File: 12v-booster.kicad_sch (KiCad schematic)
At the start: 21 parts, among them J409 12V_OUT, U201 XCL220, U405 TPS55340-Q1

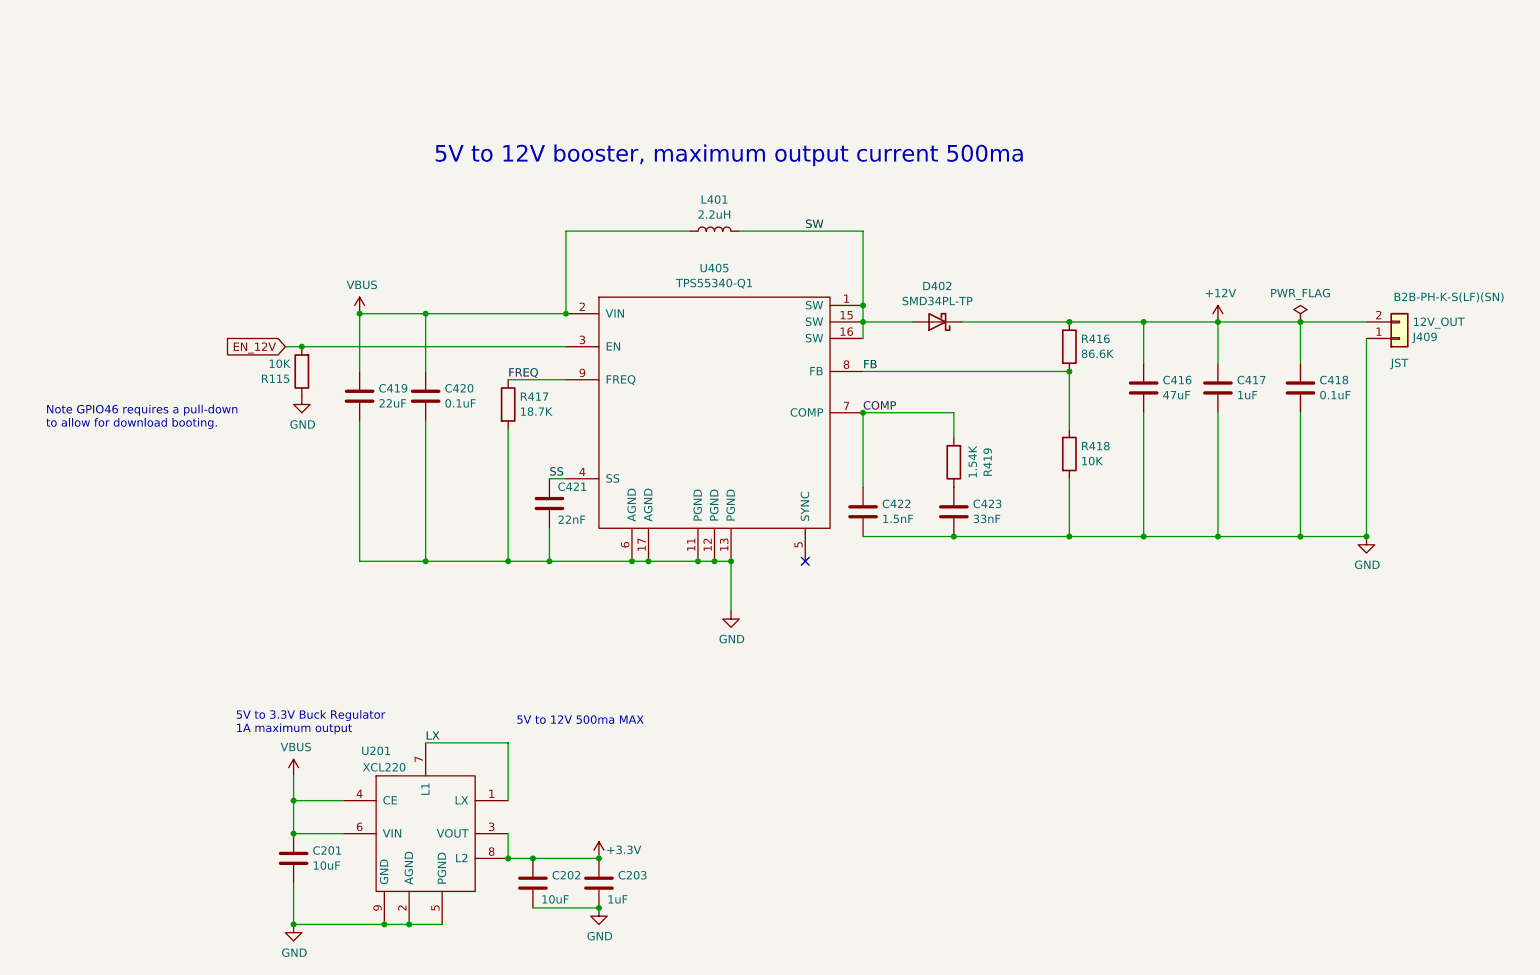
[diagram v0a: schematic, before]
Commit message: More updates
- Changed obsolete unidirectional level shifter to open-collector level shifter
- Replaced BSS138 level shifters with dedicated level shifter
- Changed all 5V I/O pins to have 33 ohm resistor in series
- Changed a few capacitors
- Cleanup tracks, vias, silkscreen, etc.

Signed-off-by: Aaron Williams <aaron.w2@gmail.com>
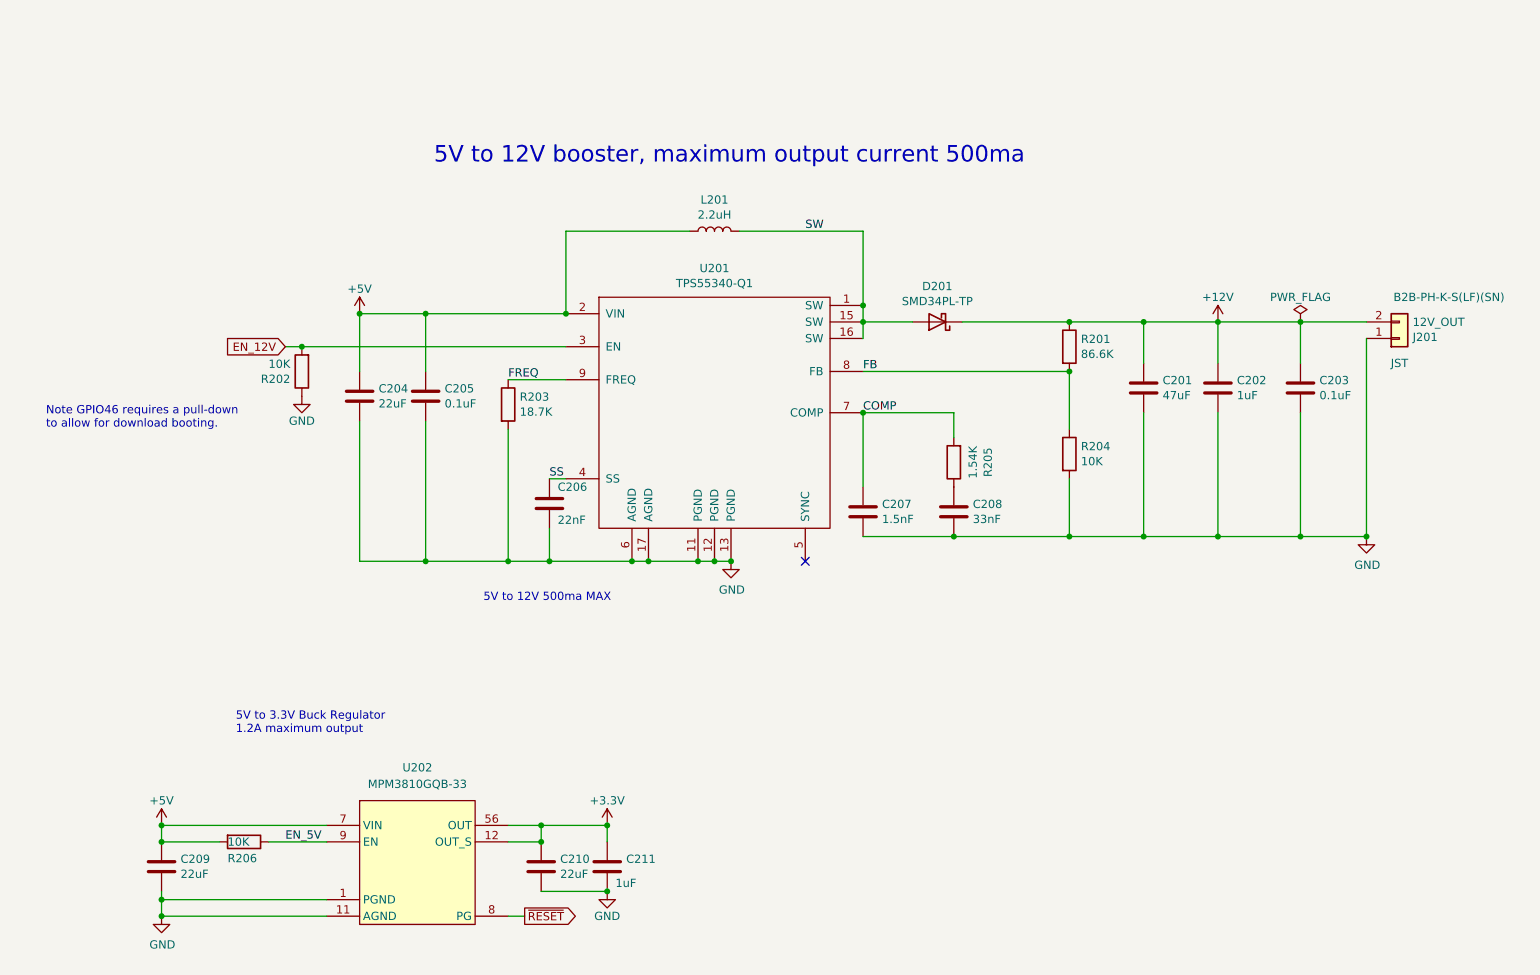
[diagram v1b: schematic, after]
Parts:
- removed C201, C202: 10uF, Capacitor_SMD:C_0603_1608Metric, symbol Device:C
- removed U201: XCL220, Torex_Semi:CL-2025-02, symbol led-controller-wrover32-rescue:XCL21X-Torex_Semiconductor
- added C209, C210: 22uF, Capacitor_SMD:C_0603_1608Metric, symbol Device:C
- added R206: 10K, Resistor_SMD:R_0402_1005Metric, symbol Device:R
- added U202: MPM3810GQB-33, Package_DFN_QFN:Monolithic_QFN-12-2.5x3.0mm_P0.4mm, symbol Power_Management:MPM3810GQB-33
- renumbered C416 to C201, C417 to C202, C418 to C203, C419 to C204, C420 to C205, C421 to C206, C422 to C207, C423 to C208, C203 to C211, D402 to D201, J409 to J201, L401 to L201, R416 to R201, R115 to R202, R417 to R203, R418 to R204, R419 to R205, U405 to U201
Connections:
- net +3V3: now also C210.1, U202.12 (OUT_S), U202.56 (OUT)
- net GND: now also C209.2, C210.2, U202.1 (PGND), U202.11 (AGND), U202.2 (PGND)
- net VBUS renamed +5V
- net +5V: now also C209.1, R206.2, U202.7 (VIN)
- new net EN_5V: R206.1, U202.9 (EN)
- new net ~{RESET}: U202.8 (PG)
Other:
- note added: "5V to 3.3V Buck Regulator 1.2A maximum output"
- note removed: "5V to 3.3V Buck Regulator 1A maximum output"
- moved on the sheet: C211

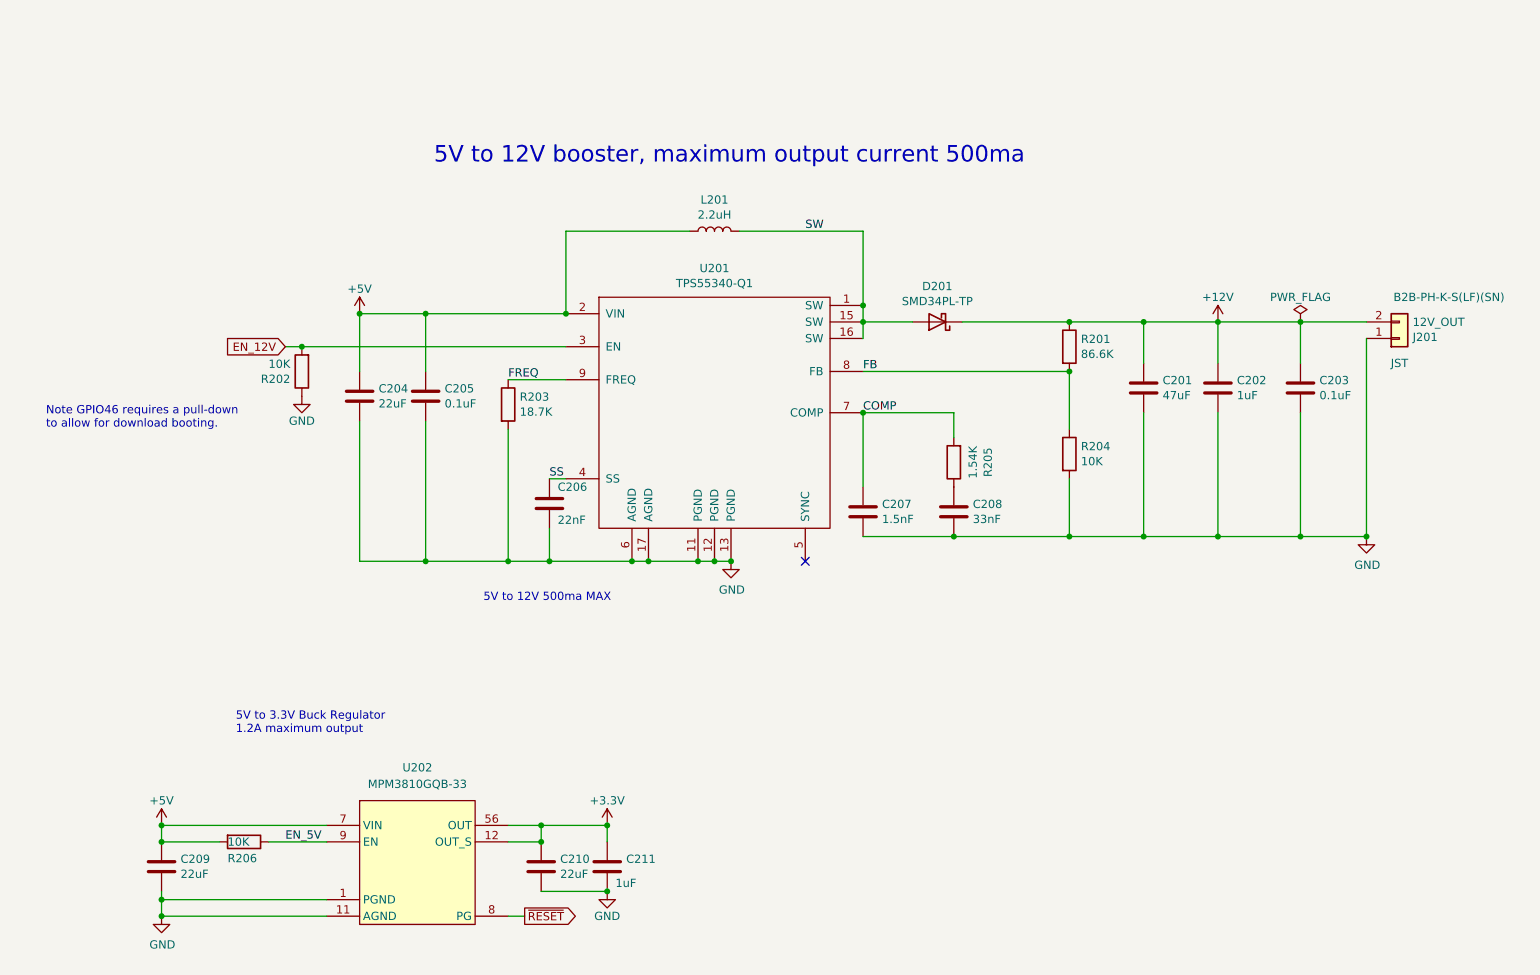
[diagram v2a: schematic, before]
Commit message: Switched to a different 12V booster chip and increased 12V from 500ma to 1A.
Also:
- Switched most 10uF capacitors to 0402 footprints.
- Other cleanup

Signed-off-by: Aaron Williams <aaron.w2@gmail.com>
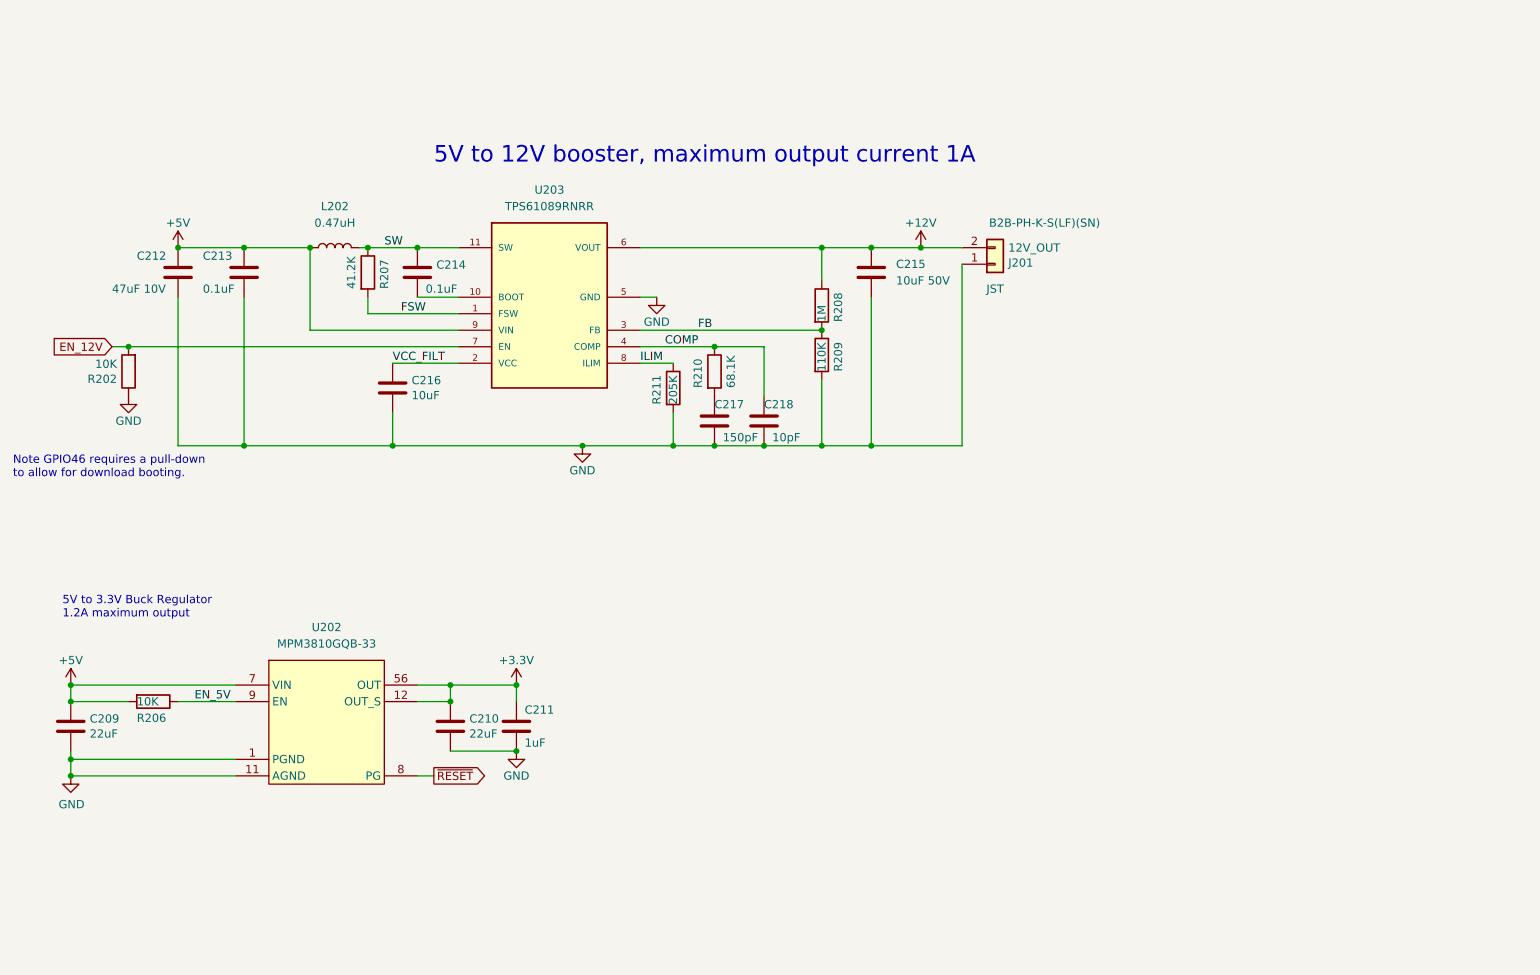
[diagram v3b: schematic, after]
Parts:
- removed C201: 47uF, Capacitor_SMD:C_1210_3225Metric, symbol Device:C
- removed C202: 1uF, Capacitor_SMD:C_0402_1005Metric, symbol Device:C
- removed C203, C205: 0.1uF, Capacitor_SMD:C_0402_1005Metric, symbol Device:C
- removed C204: 22uF, Capacitor_SMD:C_0603_1608Metric, symbol Device:C
- removed C206: 22nF, Capacitor_SMD:C_0402_1005Metric, symbol Device:C
- removed C207: 1.5nF, Capacitor_SMD:C_0402_1005Metric, symbol Device:C
- removed C208: 33nF, Capacitor_SMD:C_0402_1005Metric, symbol Device:C
- removed D201: SMD34PL-TP, Diode_SMD:D_SOD-123F, symbol Device:D_Schottky
- removed L201: 2.2uH, Inductor_SMD:L_1210_3225Metric, symbol Device:L
- removed R201: 86.6K, Resistor_SMD:R_0402_1005Metric, symbol Device:R
- removed R203: 18.7K, Resistor_SMD:R_0402_1005Metric, symbol Device:R
- removed R204: 10K, Resistor_SMD:R_0402_1005Metric, symbol Device:R
- removed R205: 1.54K, Resistor_SMD:R_0402_1005Metric, symbol Device:R
- removed U201: TPS55340-Q1, Aaron:QFN-16-1EP_3x3mm_P0.5mm_EP2.7x2.7mm_ThermalVias, symbol led-controller-wrover32-rescue:TPS55340-Q1-texas-12v-booster-rescue
- added C212: 47uF 10V, Capacitor_SMD:C_0805_2012Metric, symbol Device:C
- added C213, C214: 0.1uF, Capacitor_SMD:C_0402_1005Metric, symbol Device:C
- added C215: 10uF 50V, Capacitor_SMD:C_0805_2012Metric, symbol Device:C
- added C216: 10uF, Capacitor_SMD:C_0402_1005Metric, symbol Device:C
- added C217: 150pF, Capacitor_SMD:C_0402_1005Metric, symbol Device:C
- added C218: 10pF, Capacitor_SMD:C_0402_1005Metric, symbol Device:C
- added L202: 0.47uH, Inductor_SMD:L_Bourns_SRP3212, symbol Device:L
- added R207: 41.2K, Resistor_SMD:R_0402_1005Metric, symbol Device:R
- added R208: 1M, Resistor_SMD:R_0402_1005Metric, symbol Device:R
- added R209: 110K, Resistor_SMD:R_0402_1005Metric, symbol Device:R
- added R210: 68.1K, Resistor_SMD:R_0402_1005Metric, symbol Device:R
- added R211: 205K, Resistor_SMD:R_0402_1005Metric, symbol Device:R
- added U203: TPS61089RNRR, Package_DFN_QFN:Texas_S_VQFN-11_2.0x2.5mm_P0.5mm_Thermal, symbol Aaron:TPS61089RNRR
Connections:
- net +12V: now also C215.1, R208.1, U203.6 (VOUT)
- net +5V: now also C212.1, C213.1, L202.1, U203.9 (VIN)
- net COMP: now also C218.1, R210.1, U203.4 (COMP)
- net EN_12V: now also U203.7 (EN)
- net FB: now also R208.2, R209.1, U203.3 (FB)
- net GND: now also C212.2, C213.2, C215.2, C216.2, C217.2, C218.2, R209.2, R211.2, U203.5 (GND)
- net SW: now also C214.1, L202.2, R207.1, U203.11 (SW)
- new net: C217.1, R210.2
- new net: C214.2, U203.10 (BOOT)
- new net FSW: R207.2, U203.1 (FSW)
- new net ILIM: R211.1, U203.8 (ILIM)
- new net VCC_FILT: C216.1, U203.2 (VCC)
- no-connect marks 1 -> 0
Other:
- note added: "5V to 12V booster, maximum output current 1A"
- note removed: "5V to 12V 500ma MAX"
- note removed: "5V to 12V booster, maximum output current 500ma"
- moved on the sheet: C209, C210, C211, J201, R202, R206, U202

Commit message: Latest 4.0 settings for pcbway
Signed-off-by: Aaron Williams <aaron.w2@gmail.com>
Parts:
- removed R202: 10K, Resistor_SMD:R_0402_1005Metric, symbol Device:R
- C201: renamed from C212; SPN (none) -> 490-9961-1-ND; SPR (none) -> Digikey; SPURL (none) -> https://www.digikey.com/en/products/detail/murata-electroni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
- C203: renamed from C215; MFR (none) -> Murata Electronics; MPN (none) -> GRM21BR61H106KE43L; SPN (none) -> 490-18663-1-ND; SPR (none) -> Digikey; SPURL (none) -> https://www.digikey.com/en/products/detail/murata-electroni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
- C208: renamed from C209; DESC CAP CER 22UF 16V X5R 0603 -> 22 µF ±20% 16V Ceramic Capacitor X5R 0603 (1608 Metric); DK_Datasheet_Link (none) -> https://media.digikey.com/pdf/Data%20Sheets/Samsung%20PDFs/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; DK_Detail_Page (none) -> https://www.digikey.com/en/products/detail/samsung-electro-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; Digi-Key_PN (none) -> 1276-7076-1-ND; MANUFACTURER (none) -> Samsung Electro-Mechanics; Manufacturer (none) -> Samsung Electro-Mechanics; SPURL https://www.digikey.com/products/en/capacitors/ceramic-capa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 -> https://www.digikey.com/en/products/detail/samsung-electro-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
- C209: renamed from C210; DESC CAP CER 22UF 16V X5R 0603 -> 22 µF ±20% 16V Ceramic Capacitor X5R 0603 (1608 Metric); DK_Datasheet_Link (none) -> https://media.digikey.com/pdf/Data%20Sheets/Samsung%20PDFs/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; DK_Detail_Page (none) -> https://www.digikey.com/en/products/detail/samsung-electro-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; Digi-Key_PN (none) -> 1276-7076-1-ND; MANUFACTURER (none) -> Samsung Electro-Mechanics; Manufacturer (none) -> Samsung Electro-Mechanics; SPURL https://www.digikey.com/products/en/capacitors/ceramic-capa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 -> https://www.digikey.com/en/products/detail/samsung-electro-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
- C210: renamed from C211; DESC (none) -> CAP CER 1UF 25V X5R 0402; Digi-Key_PN (none) -> 490-GRM155R61E105MA12JCT-ND; MANUFACTURER (none) -> Murata Electronics; MFR (none) -> Murata Electronics; MPN (none) -> GRM155R61E105MA12J; Manufacturer (none) -> Murata Electronics; Manufacturer Part Number (none) -> GRM155R61E105MA12J; SPN (none) -> 490-GRM155R61E105MA12JCT-ND; SPURL (none) -> https://www.digikey.com/en/products/detail/murata-electroni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
- L201: renamed from L202; DESC (none) -> 470 nH Shielded Drum Core, Wirewound Inductor 7 A 19.2mOhm 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; DK_Datasheet_Link (none) -> https://www.bourns.com/docs/product-datasheets/srp3212.pdf; DK_Detail_Page (none) -> https://www.bourns.com/docs/product-datasheets/srp3212.pdf; Digi-Key_PN (none) -> 118-SRP3212-R47MCT-ND; MFR (none) -> Bourns Inc.; MPN (none) -> SRP3212-R47M; Manufacturer (none) -> Bourns Inc.; Manufacturer Part Number (none) -> SRP3212-R47M; SPN (none) -> 118-SRP3212-R47MCT-ND; SPR (none) -> Digikey; SPURL (none) -> https://www.bourns.com/docs/product-datasheets/srp3212.pdf; Status (none) -> Active
- R201: renamed from R207; SPN 541-2979-1-ND -> (none); SPR Digikey -> (none); SPURL https://www.digikey.com/products/en?keywords=541-2979-1-ND -> (none)
- R204: renamed from R209; DESC 100 kOhms ±1% 0.063W, 1/16W Chip Resistor 0402 (1005 Metric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 -> (none); MFR YAGEO -> (none); MPN RC0402FR-07100KL -> (none); SPN 311-100KLRCT-ND -> (none); SPR Digikey -> (none)
- R206: DESC (none) -> 10 kOhms ±1% 0.063W, 1/16W Chip Resistor 0402 (1005 Metric)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; Digi-Key_PN (none) -> 311-10.0KLRCT-ND; MANUFACTURER (none) -> YAGEO; MFR (none) -> YAGEO; MPN (none) -> RC0402FR-0710KL; Manufacturer (none) -> YAGEO; Manufacturer Part Number (none) -> RC0402FR-0710KL; SPN 541-2979-1-ND -> 311-10.0KLRCT-ND; SPURL https://www.digikey.com/products/en?keywords=541-2979-1-ND -> https://www.digikey.com/en/products/detail/yageo/RC0402FR-0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
- U201: renamed from U203; MFR (none) -> Texas Instruments; MPN (none) -> TPS61089RNRR; SPN (none) -> 296-47295-1-ND; SPR (none) -> Digikey; SPURL (none) -> https://www.digikey.com/en/products/detail/texas-instrument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
- U202: MFR (none) -> Monolithic Power Systems Inc.; MPN (none) -> MPM3810GQB-33-Z; SPN (none) -> 1589-MPM3810GQB-33-ZCT-ND; SPR (none) -> Digikey; SPURL (none) -> https://www.digikey.com/en/products/detail/monolithic-power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
- renumbered C214 to C202, C213 to C204, C216 to C205, C217 to C206, C218 to C207, R208 to R202, R210 to R203, R211 to R205
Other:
- note removed: "Note GPIO46 requires a pull-down to allow for download booting."
- moved on the sheet: C201, C202, C203, C204, C205, C206, C207, J201, L201, R201, R202, R203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
